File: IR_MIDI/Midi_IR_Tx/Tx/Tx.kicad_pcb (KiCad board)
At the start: 2 copper layers, 97.2 x 50.6 mm, 30 parts, among them J1 MIDI in, J2 MIDI Thr, J3 Power In, J4 FanPower, Q1 PSMNR56-25YLEX, U1 MCP14E3, Y1 1MHz

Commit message: some cad work and updated midi note charts
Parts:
- moved REF** 1.49 mm to (224.0, 120.9)
- moved REF** 1.36 mm to (136.3, 120.9)
- moved REF** 1.28 mm to (224.0, 79.8)
- moved REF** 1.10 mm to (136.3, 79.8)
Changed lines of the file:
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@@
 	(footprint "MountingHole:MountingHole_3.2mm_M3_DIN965_Pad"
 		(layer "F.Cu")
-		(at 225 79)
+		(at 224 79.8)
 		(descr "Mounting Hole 3.2mm, M3, generated by kicad-footprint-generator mountinghole.py")
 		(tags "mountinghole M3 DIN965")
@@
 	(footprint "MountingHole:MountingHole_3.2mm_M3_DIN965_Pad"
 		(layer "F.Cu")
-		(at 135.5 79.05)
+		(at 136.3 79.8)
 		(descr "Mounting Hole 3.2mm, M3, generated by kicad-footprint-generator mountinghole.py")
 		(tags "mountinghole M3 DIN965")
@@
 	(footprint "MountingHole:MountingHole_3.2mm_M3_DIN965_Pad"
 		(layer "F.Cu")
-		(at 225 122)
+		(at 224 120.9)
 		(descr "Mounting Hole 3.2mm, M3, generated by kicad-footprint-generator mountinghole.py")
 		(tags "mountinghole M3 DIN965")
@@
 	(footprint "MountingHole:MountingHole_3.2mm_M3_DIN965_Pad"
 		(layer "F.Cu")
-		(at 135.5 122)
+		(at 136.3 120.9)
 		(descr "Mounting Hole 3.2mm, M3, generated by kicad-footprint-generator mountinghole.py")
 		(tags "mountinghole M3 DIN965")
@@
 		(layer "Edge.Cuts")
 	)
+	(gr_rect
+		(start 224 75.05)
+		(end 228.79 79.8)
+		(stroke
+			(width 0.1)
+			(type default)
+		)
+		(fill no)
+		(layer "F.Fab")
+	)
+	(gr_rect
+		(start 131.54 120.9)
+		(end 136.3 125.6805)
+		(stroke
+			(width 0.1)
+			(type default)
+		)
+		(fill no)
+		(layer "F.Fab")
+	)
+	(gr_rect
+		(start 224 120.9)
+		(end 228.79 125.6805)
+		(stroke
+			(width 0.1)
+			(type default)
+		)
+		(fill no)
+		(layer "F.Fab")
+	)
+	(gr_rect
+		(start 131.54 75.05)
+		(end 136.3 79.8)
+		(stroke
+			(width 0.1)
+			(type default)
+		)
+		(fill no)
+		(layer "F.Fab")
+	)
 	(gr_text "Ifrared MIDI Transmitter\nBoard Rev. A\nFall 2025"
 		(at 133 100.36525 270)
@@
 			(keep_text_aligned yes)
 		)
-		(gr_text "3828.7402 mils"
+		(gr_text "3.8287 in"
 			(at 180.165 135.85 0)
 			(layer "F.Fab")
@@
 			(keep_text_aligned yes)
 		)
-		(gr_text "1993.3268 mils"
+		(gr_text "1.9933 in"
 			(at 240.85 100.36525 90)
 			(layer "F.Fab")

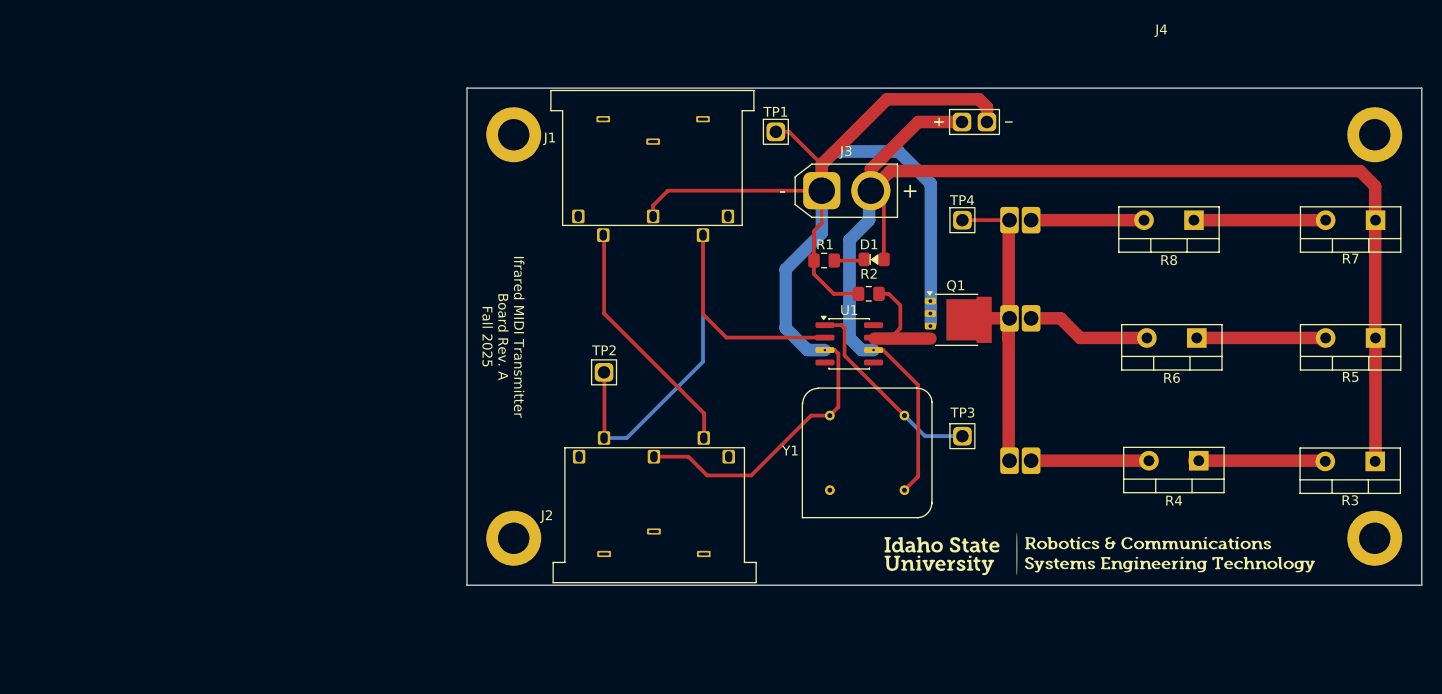
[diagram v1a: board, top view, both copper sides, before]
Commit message: revised IR Tx board
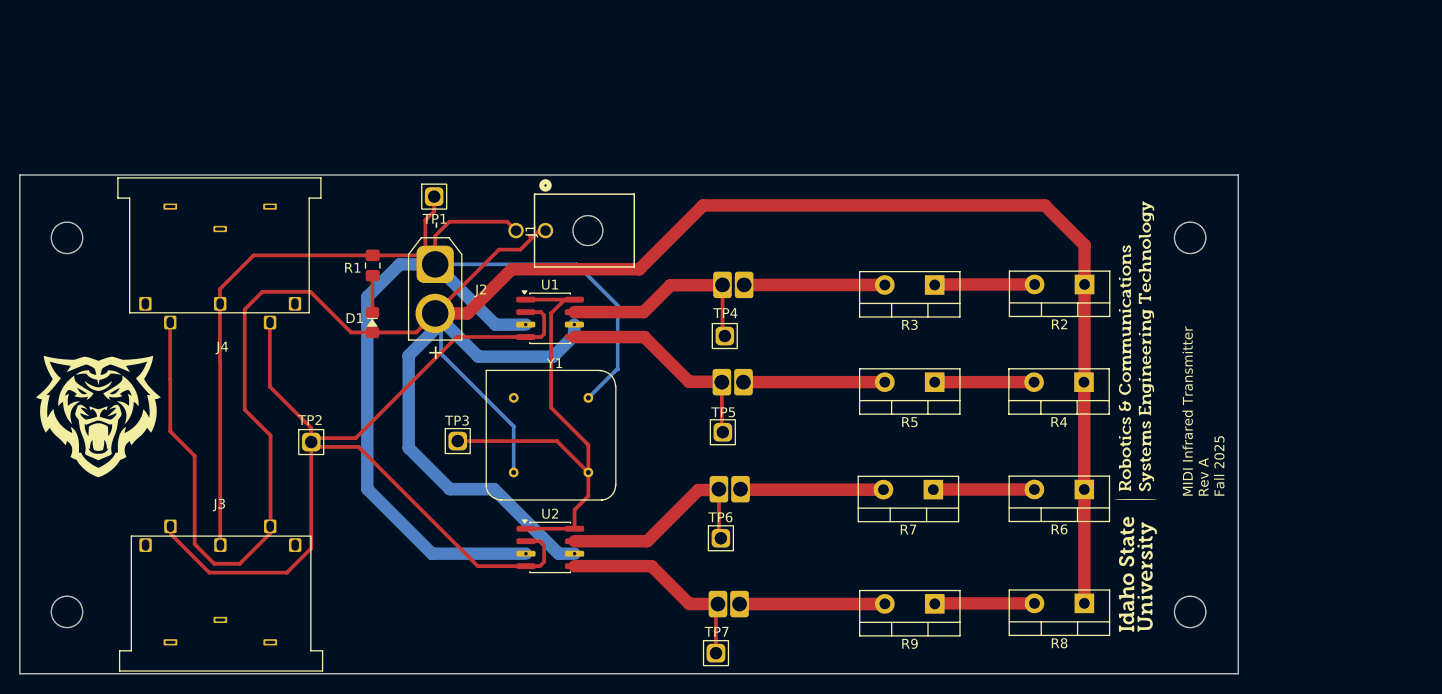
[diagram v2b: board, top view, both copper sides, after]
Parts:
- removed the G*** at (215.0, 96.5)
- removed Q1: PSMNR56-25YLEX, Package_TO_SOT_SMD:LFPAK56
- removed the REF** at (224.0, 79.8)
- removed the REF** at (136.3, 79.8)
- removed the REF** at (224.0, 120.9)
- removed the REF** at (136.3, 120.9)
- added D5: D_Filled, 2JB_Footprints:Fat_2Pin_D, B.Cu at (159.0, 125.3)
- added G***: LOGO, 2JB_Logos:Bengal_Head_0_5x0_5, F.Cu at (94.0, 108.5)
- added R9: 2Ω, Package_TO_SOT_THT:TO-220-2_Vertical, F.Cu at (179.2, 127.6)
- added REF**: MountingHole_3.2mm_M3, MountingHole:MountingHole_3.2mm_M3, F.Cu at (90.8, 128.4)
- added REF**: MountingHole_3.2mm_M3, MountingHole:MountingHole_3.2mm_M3, F.Cu at (205.2, 90.3)
- added REF**: MountingHole_3.2mm_M3, MountingHole:MountingHole_3.2mm_M3, F.Cu at (205.2, 128.4)
- added REF**: MountingHole_3.2mm_M3, MountingHole:MountingHole_3.2mm_M3, F.Cu at (90.8, 90.3)
- added TP5: IR2, 2JB_Footprints:1X1_100mil_Header, F.Cu at (177.9, 110.1)
- added TP6: IR3, 2JB_Footprints:1X1_100mil_Header, F.Cu at (177.7, 120.9)
- added TP7: IR4, 2JB_Footprints:1X1_100mil_Header, F.Cu at (177.2, 132.6)
- added U2: MCP14E3, Package_SO:SOIC-8_3.9x4.9mm_P1.27mm, F.Cu at (140.0, 121.8)
- J1: value MIDI in -> FanPower; footprint 2JB_Footprints:DIN-5PIN_MIDI -> 2JB_Footprints:2PinMolex
- J2: value MIDI Thr -> Power In; footprint 2JB_Footprints:DIN-5PIN_MIDI -> Connector_AMASS:AMASS_XT30U-F_1x02_P5.0mm_Vertical
- J3: value Power In -> MIDI Thr; footprint Connector_AMASS:AMASS_XT30U-F_1x02_P5.0mm_Vertical -> 2JB_Footprints:DIN-5PIN_MIDI
- J4: value FanPower -> MIDI in; footprint 2JB_Footprints:1X2_100mil_Header -> 2JB_Footprints:DIN-5PIN_MIDI
- R2: value 10KΩ -> 2Ω; footprint 2JB_Footprints:C_0805 -> Package_TO_SOT_THT:TO-220-2_Vertical
- TP4: value SignalOut -> IR1
- moved J4 94.5 mm to (108.6, 91.4), turned to -90 degrees
- moved J3 75.9 mm to (104.2, 127.2), turned to 90 degrees
- moved G*** 57.4 mm to (114.4, 109.8), turned to 0 degrees
- moved R7 52.7 mm to (179.0, 116.0)
- moved D1 52.5 mm to (121.1, 99.2), turned to 90 degrees
- moved TP3 51.4 mm to (150.9, 111.0)
- moved R3 48.3 mm to (179.2, 95.1)
- moved R1 46.0 mm to (121.9, 93.1), turned to 90 degrees
- moved R5 45.1 mm to (179.2, 105.0)
- moved D4 42.5 mm to (159.0, 113.6)
- moved R8 40.6 mm to (194.4, 127.5)
- moved Y1 35.5 mm to (133.5, 103.8), turned to 0 degrees
- moved TP1 35.4 mm to (148.5, 86.1)
- moved D2 32.8 mm to (159.2, 92.9)
- moved J2 32.2 mm to (128.3, 93.0), turned to -90 degrees
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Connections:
- D1 pad 2: Net-(D1-A) -> Net-(U1-VCC)
- D3 pad 2: Net-(D2-K) -> Net-(D3-K)
- D4 pad 2: Net-(D2-K) -> Net-(D4-K)
- J1 pad 1: unconnected-(J1-Pad1) -> Net-(U1-VCC)
- J2 pad 1: unconnected-(J2-Pad1) -> GND
- J2 pad 2: GND -> Net-(U1-VCC)
- J3 pad 1: GND -> unconnected-(J3-Pad1)
- J3 pad 2: Net-(U1-VCC) -> GND
- J4 pad 1: Net-(U1-VCC) -> unconnected-(J4-Pad1)
- R2 pad 1: Net-(Q1-G) -> Net-(U1-VCC)
- R2 pad 2: GND -> Net-(R2-Pad2)
- R3 pad 1: Net-(U1-VCC) -> Net-(R2-Pad2)
- R3 pad 2: Net-(R3-Pad2) -> Net-(D2-A)
- R4 pad 1: Net-(R3-Pad2) -> Net-(U1-VCC)
- R4 pad 2: Net-(D2-A) -> Net-(R4-Pad2)
- R5 pad 1: Net-(U1-VCC) -> Net-(R4-Pad2)
- R5 pad 2: Net-(R5-Pad2) -> Net-(D3-A)
- R6 pad 1: Net-(R5-Pad2) -> Net-(U1-VCC)
- R6 pad 2: Net-(D3-A) -> Net-(R6-Pad2)
- R7 pad 1: Net-(U1-VCC) -> Net-(R6-Pad2)
- R7 pad 2: Net-(R7-Pad2) -> Net-(D4-A)
- R8 pad 1: Net-(R7-Pad2) -> Net-(U1-VCC)
- R8 pad 2: Net-(D4-A) -> Net-(R8-Pad2)
- U1 pad 4: unconnected-(U1-INB-Pad4) -> Net-(U1-INA)
- U1 pad 5: unconnected-(U1-~{OUTB}-Pad5) -> Net-(D3-K)
- U1 pad 7: Net-(Q1-G) -> Net-(D2-K)
- U1 pad 8: unconnected-(U1-ENB-Pad8) -> Net-(U1-ENA)
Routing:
- net Net-(U1-VCC): track 137.8 -> 277.7 mm
- net Net-(U1-INA): track 54.3 -> 106.4 mm
- net Net-(U1-ENA): track 20.3 -> 51.6 mm
- net Net-(J1-Pad4): track 24.8 -> 0.00 mm
- net Net-(D4-K): track 0.00 -> 21.7 mm
- net Net-(D3-K): track 0.00 -> 21.3 mm
- net Net-(D5-K): track 0.00 -> 21.0 mm
- net Net-(D2-K): track 36.1 -> 20.9 mm
- net Net-(D5-A): track 0.00 -> 14.8 mm
- net GND: track 143.2 -> 157.7 mm
- net Net-(Q1-G): track 13.8 -> 0.00 mm
- net Net-(R3-Pad2): track 13.4 -> 0.00 mm
- net Net-(R5-Pad2): track 13.3 -> 0.00 mm
- net Net-(R7-Pad2): track 13.3 -> 0.00 mm
- net Net-(R6-Pad2): track 0.00 -> 10.3 mm
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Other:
- board size 97.2 x 50.6 mm -> 124.1 x 50.8 mm
- board text added: "MIDI Infrared Transmitter Rev A Fall 2025"
- board text removed: "Ifrared MIDI Transmitter Board Rev. A Fall 2025"
